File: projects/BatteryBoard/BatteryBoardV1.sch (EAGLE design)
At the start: 3 parts, among them U1 LTC4412MPS6

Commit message: Updates to Battery charging solar panel front end and start of charging schematics. Updates to BSE library
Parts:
- added C3: 10uF, BrownSpaceEngineering:CAP0805
- added D1, D2, D3, D4, D5, D6: DFLS130L, BrownSpaceEngineering:DFLS130L
- added M1: BSO201SP, BrownSpaceEngineering:BSO201SP
- added R1, R10, R2, R3, R4, R5, R6, R7, R8, R9: 0R, BrownSpaceEngineering:RES0805
- added R11: 10R, BrownSpaceEngineering:RES0805
- added R12: 0, BrownSpaceEngineering:RES0805
- added R13: 40K, BrownSpaceEngineering:RES0805
- added R14, R15, R16, R17, R18, R19, R20: 10K, BrownSpaceEngineering:RES0805
- added U2: SM74611, BrownSpaceEngineering:SM74611
- added U3, U4: LTC4121, BrownSpaceEngineering:LTC4121
- C2: value (none) -> 0.1uF
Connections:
- net SP_1_ST renamed SP_F_ST
- removed net SP_1: C1.P$1, U1.VIN
- new net 3V3: R17.2, R18.2, R19.2, R20.2
- new net LION1_CHGN: R17.1, U3.~CHRG
- new net LION1_FAULTN: R18.1, U3.~FAULT
- new net LION1_RUN_CHG: R15.2, U3.RUN
- new net LION2_CHGN: R19.1, U4.~CHRG
- new net LION2_FAULTN: R20.1, U4.~FAULT
- new net LION2_RUN_CHG: R16.2, U4.RUN
- new net N$1: M1.G, U1.GATE
- new net N$2: C2.P$1, M1.S, R4.1, U1.SNS
- new net N$3: R1.2, U2.A
- new net N$4: R3.1, U2.C
- new net N$5: C1.P$1, M1.D, R2.2, U1.VIN
- new net N$6: U3.BAT
- new net N$7: U4.BAT
- new net PANELREF: R13.1, R14.2
- new net SP_C: D1.C, D2.C, D3.C, D4.C, D5.C, R1.1, R10.2, R2.1, R5.1, R6.2, R7.2, R8.2, R9.2
- new net SP_C_O: R11.1, R12.1, R3.2, R4.2, R5.2
- new net SP_OUT: C3.P$1, D6.C, R11.2, R12.2, R13.2, R15.1, R16.1, U3.IN, U4.IN
- new net SP_X_N: D2.A, R7.1
- new net SP_X_P: D1.A, R6.1
- new net SP_Y_N: D5.A, R10.1
- new net SP_Z_N: D4.A, R9.1
- new net SP_Z_P: D3.A, R8.1
- new net UMB_CHG: D6.A
- net GND: now also C2.P$2, C3.P$2, R14.1, U4.GND
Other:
- note added: "Combined Solar Panel Input Option"
- note added: "Current Sense Option"
- note added: "Solar Panel Input Option"

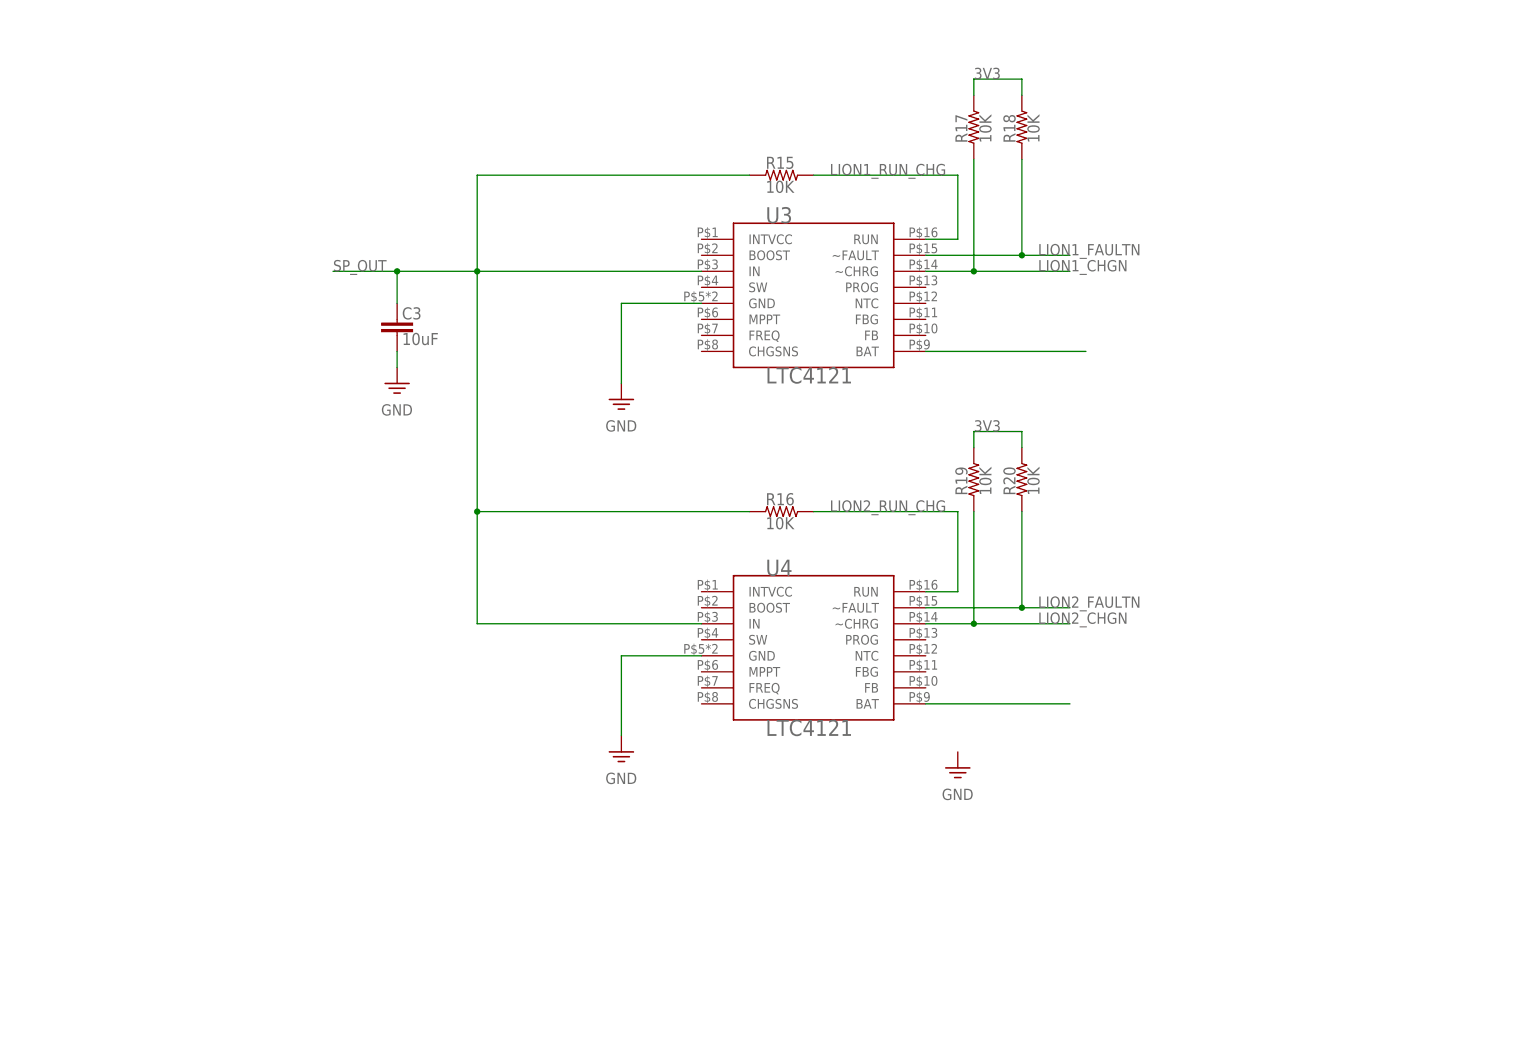
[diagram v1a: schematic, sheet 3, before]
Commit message: Battery Board Li-Ion charging circuit finished.
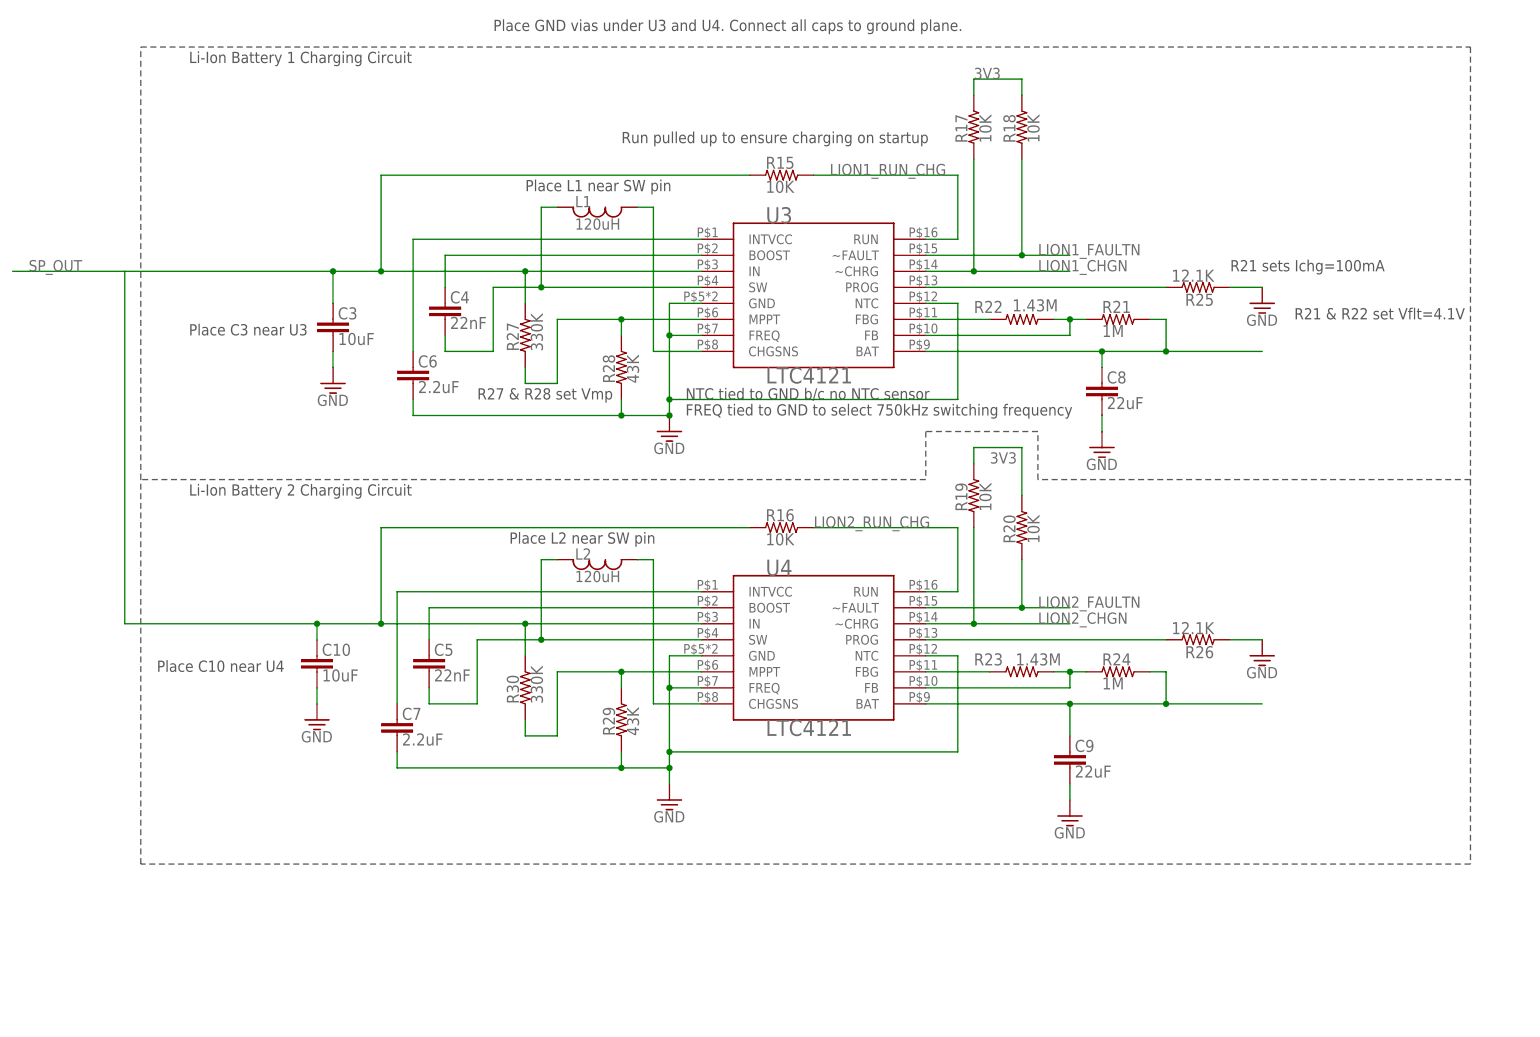
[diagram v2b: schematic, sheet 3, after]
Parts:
- added C10: 10uF, BrownSpaceEngineering:CAP0805
- added C4, C5: 22nF, BrownSpaceEngineering:CAP0805
- added C6, C7: 2.2uF, BrownSpaceEngineering:CAP0805
- added C8, C9: 22uF, BrownSpaceEngineering:CAP0805
- added L1, L2: 120uH, BrownSpaceEngineering:IND1812
- added R21, R24: 1M, BrownSpaceEngineering:RES0805
- added R22, R23: 1.43M, BrownSpaceEngineering:RES0805
- added R25, R26: 12.1K, BrownSpaceEngineering:RES0805
- added R27, R30: 330K, BrownSpaceEngineering:RES0805
- added R28, R29: 43K, BrownSpaceEngineering:RES0805
- added V1: UMB_CHG, BrownSpaceEngineering:VIA60MIL
- added V2: SP_X_P, BrownSpaceEngineering:VIA60MIL
- added V3: SP_X_N, BrownSpaceEngineering:VIA60MIL
- added V4: SP_Z_P, BrownSpaceEngineering:VIA60MIL
- added V5: SP_Z_N, BrownSpaceEngineering:VIA60MIL
- added V6: SP_Y_N, BrownSpaceEngineering:VIA60MIL
- added V7: SP_C_O, BrownSpaceEngineering:VIA60MIL
- added V8: SP_OUT, BrownSpaceEngineering:VIA60MIL
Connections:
- new net N$10: C5.P$1, U4.BOOST
- new net N$11: C5.P$2, L2.P$1, U4.SW
- new net N$12: C7.P$1, U4.INTVCC
- new net N$13: C6.P$1, U3.INTVCC
- new net N$14: R23.1, U4.FBG
- new net N$15: R23.2, R24.1, U4.FB
- new net N$16: R22.1, U3.FBG
- new net N$17: R21.1, R22.2, U3.FB
- new net N$18: L1.P$2, U3.CHGSNS
- new net N$19: R25.2, U3.PROG
- new net N$20: R26.2, U4.PROG
- new net N$21: R29.2, R30.1, U4.MPPT
- new net N$22: R27.1, R28.2, U3.MPPT
- new net N$23: L2.P$2, U4.CHGSNS
- new net N$8: C4.P$2, L1.P$1, U3.SW
- new net N$9: C4.P$1, U3.BOOST
- net GND: now also C10.P$2, C6.P$2, C7.P$2, C8.P$2, C9.P$2, R25.1, R26.1, R28.1, R29.1, U3.FREQ, U3.NTC, U4.FREQ, U4.NTC
- net N$6: now also C8.P$1, R21.2
- net N$7: now also C9.P$1, R24.2
- net SP_C_O: now also V7.P$1
- net SP_OUT: now also C10.P$1, R27.2, R30.2, V8.P$1
- net SP_X_N: now also V3.P$1
- net SP_X_P: now also V2.P$1
- net SP_Y_N: now also V6.P$1
- net SP_Z_N: now also V5.P$1
- net SP_Z_P: now also V4.P$1
- net UMB_CHG: now also V1.P$1
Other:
- note added: "FREQ tied to GND to select 750kHz switching frequency"
- note added: "Li-Ion Battery 1 Charging Circuit"
- note added: "Li-Ion Battery 2 Charging Circuit"
- note added: "NTC tied to GND b/c no NTC sensor"
- note added: "Place C10 near U4"
- note added: "Place C3 near U3"
- note added: "Place GND vias under U3 and U4. Connect all caps to ground plane."
- note added: "Place L1 near SW pin"
- note added: "Place L2 near SW pin"
- note added: "R21 & R22 set Vflt=4.1V"
- note added: "R21 sets Ichg=100mA"
- note added: "R27 & R28 set Vmp"
- note added: "Run pulled up to ensure charging on startup"
- moved on the sheet: C2, C3, M1, R16, R19, R20, R4

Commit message: Li-ion batteries added to battery charging
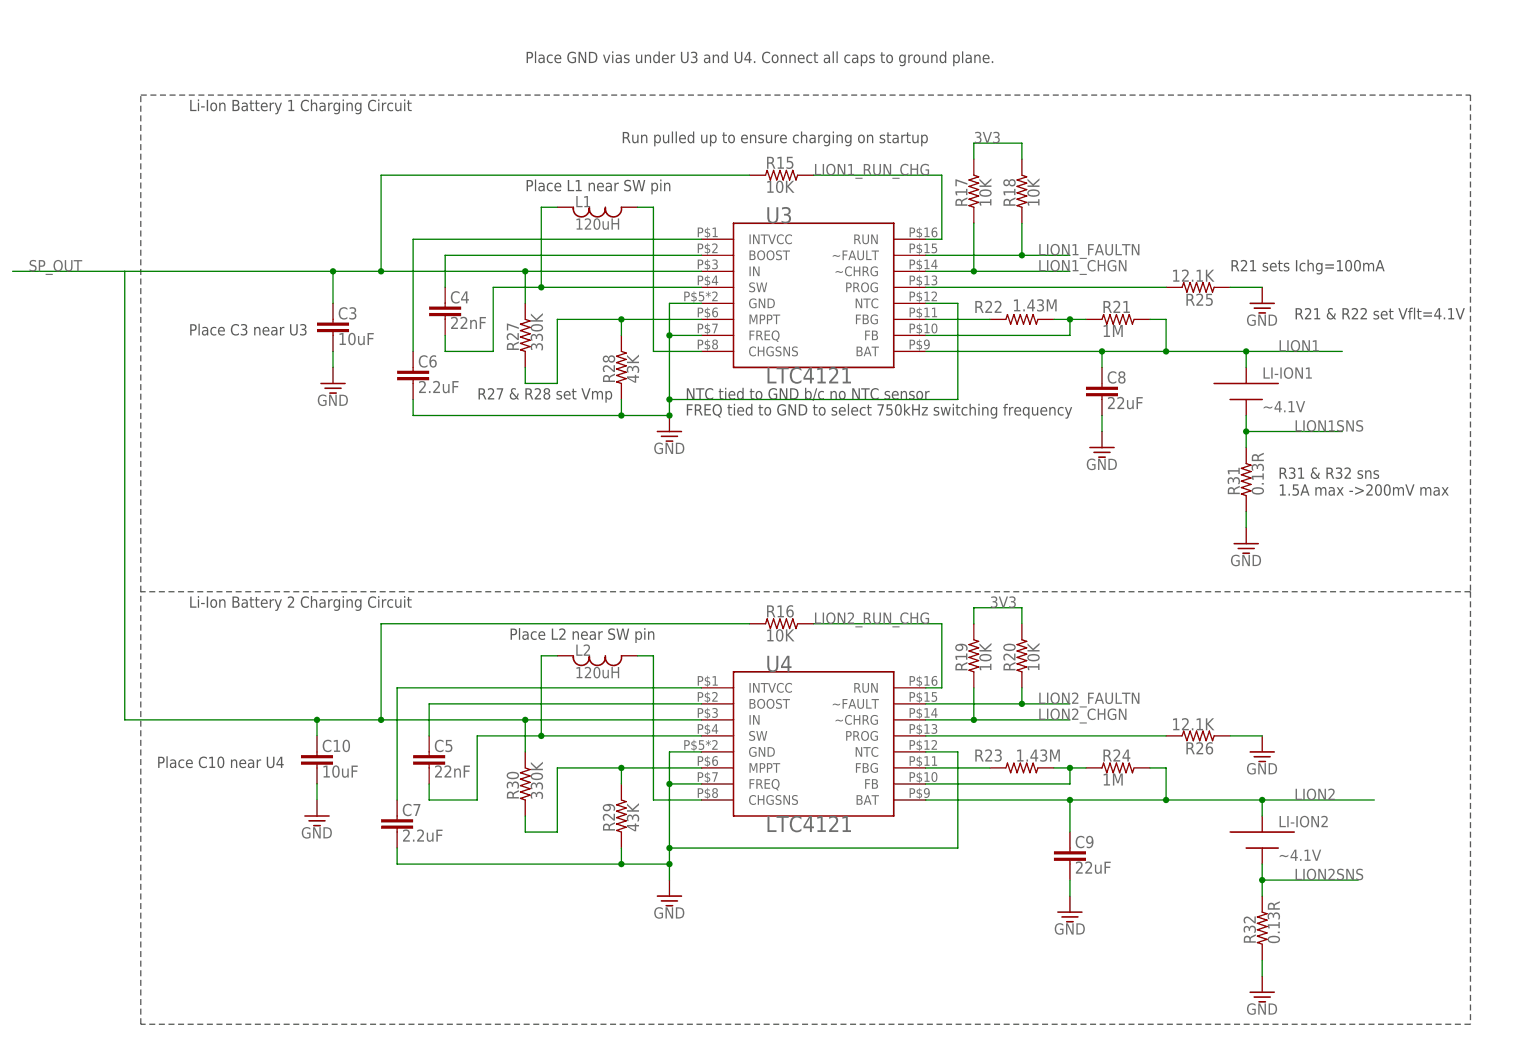
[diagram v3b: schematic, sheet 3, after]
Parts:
- added LI-ION1, LI-ION2: ~4.1V, BrownSpaceEngineering:LI-ION
- added R31, R32: 0.13R, BrownSpaceEngineering:RES0805
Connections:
- removed net N$6: C8.P$1, R21.2, U3.BAT
- removed net N$7: C9.P$1, R24.2, U4.BAT
- new net LION1: C8.P$1, LI-ION1.PLUS, R21.2, U3.BAT
- new net LION1SNS: LI-ION1.MINUS, R31.2
- new net LION2: C9.P$1, LI-ION2.PLUS, R24.2, U4.BAT
- new net LION2SNS: LI-ION2.MINUS, R32.2
- net GND: now also R31.1, R32.1
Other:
- note added: "R31 & R32 sns 1.5A max ->200mV max"
- moved on the sheet: C10, C5, C7, C9, L2, R16, R17, R18, R19, R20, R23, R24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

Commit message: Added Battery Board Li-Ion Diode ORing and began LiFePO4 charging circuitry
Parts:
- added C11, C12: 4.7uF, BrownSpaceEngineering:CAP0805
- added C13, C14: 1uF, BrownSpaceEngineering:CAP0805
- added LIFEPO1, LIFEPO2: ~3.5V, BrownSpaceEngineering:LIFEPO4
- added R33, R35, R39: 150K, BrownSpaceEngineering:RES0805
- added R34, R36, R40, R44, R48, R50: 100K, BrownSpaceEngineering:RES0805
- added R37, R38: 470K, BrownSpaceEngineering:RES0805
- added R41: 0.002R, BrownSpaceEngineering:RES0805
- added R42, R43: 10K, BrownSpaceEngineering:RES0805
- added R45: 330K, BrownSpaceEngineering:RES0805
- added R46: 43K, BrownSpaceEngineering:RES0805
- added R47: 95K, BrownSpaceEngineering:RES0805
- added R49: 287K, BrownSpaceEngineering:RES0805
- added U$1, U$2: LTC4411, BrownSpaceEngineering:LTC4411
- added U5: LTC4121, BrownSpaceEngineering:LTC4121
- added V10: LION1_RUN_CHG, BrownSpaceEngineering:VIA60MIL
- added V11: LION1_FAULTN, BrownSpaceEngineering:VIA60MIL
- added V12: LION1_CHGN, BrownSpaceEngineering:VIA60MIL
- added V13: LION1REF, BrownSpaceEngineering:VIA60MIL
- added V14: LIFEB1SNS, BrownSpaceEngineering:VIA60MIL
- added V9: LION1SNS, BrownSpaceEngineering:VIA60MIL
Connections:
- new net LIFE1REF: R49.2, R50.2
- new net LIFE2REF: R47.1, R48.2
- new net LIFEB1SNS: LIFEPO2.MINUS, R41.2, V14.P$1
- new net LIFE_B1_CHGN: R42.1
- new net LIFE_B1_FAULTN: R43.1
- new net LIFE_B1_RUNCHG: R44.2, U5.RUN
- new net LION1REF: R33.1, R34.2, V13.P$1
- new net LION1_RUN_DISG: U$1.CNTRL
- new net LION1_STAT: R37.1, U$1.STAT
- new net LION2REF: R35.1, R36.2
- new net LION2_RUN_DISG: U$2.CNTRL
- new net LION2_STAT: R38.1, U$2.STAT
- new net LIONREF: R39.1, R40.2
- new net LION_OUT: C11.P$1, C12.P$1, R39.2, U$1.OUT, U$2.OUT
- new net N$24: LIFEPO1.MINUS, LIFEPO2.PLUS, R47.2
- new net N$25: LIFEPO1.PLUS, R49.1, U5.BAT
- new net N$27: R45.1, R46.2, U5.MPPT
- net 3V3: now also R37.2, R38.2, R42.2, R43.2
- net GND: now also C11.P$2, C12.P$2, C13.P$1, C14.P$1, R34.1, R36.1, R40.1, R41.1, R44.1, R46.1, R48.1, R50.1, U$1.GND, U$2.GND, U5.GND, U5.NTC
- net LION1: now also C13.P$2, R33.2, U$1.IN
- net LION1SNS: now also V9.P$1
- net LION1_CHGN: now also V12.P$1
- net LION1_FAULTN: now also V11.P$1
- net LION1_RUN_CHG: now also V10.P$1
- net LION2: now also C14.P$2, R35.2, U$2.IN
- net SP_OUT: now also R45.2, U5.IN
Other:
- note added: "Internal Pull-downs in LTC4411 ensure default "on" operation."
- note added: "LTC4121 can handle several amps of inrush current upon battery connection"
- note added: "Li-Ion Battery 1 Ideal Diode OR"
- note added: "Li-Ion Battery 2 Ideal Diode OR"
- note added: "Place GND vias under U3 and U4. Connect all caps to ground plane. VIAs added for debugging circuit functionality."
- note removed: "Place GND vias under U3 and U4. Connect all caps to ground plane."

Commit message: Continued work on LiFePO4 charging and library updates
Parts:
- added C15: 2.2uF, BrownSpaceEngineering:CAP0805
- added C16: 22nF, BrownSpaceEngineering:CAP0805
- added C17: 10uF, BrownSpaceEngineering:CAP0805
- added C18: 22uF, BrownSpaceEngineering:CAP0805
- added L3: 120uH, BrownSpaceEngineering:IND1812
- added R51: 12.1K, BrownSpaceEngineering:RES0805
- added R52: 887K, BrownSpaceEngineering:RES0805
- added R53: 1.74M, BrownSpaceEngineering:RES0805
- added V15: LIFE_B1_RUNCHG, BrownSpaceEngineering:VIA60MIL
- added V16: LIFE2, BrownSpaceEngineering:VIA60MIL
- added V17: LIFE1, BrownSpaceEngineering:VIA60MIL
- added V18: LIFE_B1_CHGN, BrownSpaceEngineering:VIA60MIL
- added V19: LIFE_B1_FAULTN, BrownSpaceEngineering:VIA60MIL
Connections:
- removed net N$24: LIFEPO1.MINUS, LIFEPO2.PLUS, R47.2
- removed net N$25: LIFEPO1.PLUS, R49.1, U5.BAT
- new net LIFE1: C18.P$1, LIFEPO1.PLUS, R49.1, R53.2, U5.BAT, V17.P$1
- new net LIFE2: LIFEPO1.MINUS, LIFEPO2.PLUS, R47.2, V16.P$1
- new net N$26: R52.1, U5.FBG
- new net N$28: R52.2, R53.1, U5.FB
- new net N$29: C15.P$2, U5.INTVCC
- new net N$30: C16.P$1, L3.P$2, U5.SW
- new net N$31: C16.P$2, U5.BOOST
- new net N$32: L3.P$1, U5.CHGSNS
- new net N$7: R51.1, U5.PROG
- net GND: now also C15.P$1, C17.P$1, C18.P$2, R51.2, U5.FREQ
- net LIFE_B1_CHGN: now also V18.P$1
- net LIFE_B1_FAULTN: now also V19.P$1
- net LIFE_B1_RUNCHG: now also V15.P$1
- net SP_OUT: now also C17.P$2
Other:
- note added: "TODO: FUSE, BLOCKING PMOS (X2?) OUTPUTSNS"
- note added: "TODO: SWITCHING FOR BALANCING"

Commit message: Some minor updates
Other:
- note added: "TODO: Data managment and I/O."
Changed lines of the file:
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@@
 <description>Data and I/O</description>
 <plain>
+<text x="12.7" y="12.7" size="1.778" layer="97">TODO: Data managment and I/O.</text>
 </plain>
 <instances>
@@
 <plain>
 <text x="180.34" y="53.34" size="1.778" layer="97">TODO: FUSE, BLOCKING PMOS (X2?) OUTPUTSNS</text>
-<text x="99.06" y="15.24" size="1.778" layer="97">TODO: SWITCHING FOR BALANCING</text>
+<text x="60.96" y="17.78" size="1.778" layer="97">TODO: SWITCHING FOR BALANCING</text>
 </plain>
 <instances>
